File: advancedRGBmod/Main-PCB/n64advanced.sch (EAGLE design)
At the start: 110 parts, among them J5 2510-, J6 UPS, U1 10CL010YE144, U2 ADV7125/ADV7123, U4 74LVC3G17, U5 S25FLXXXSO8-DUAL, U6 TLV70012DDC, U7 TLV70025DDC

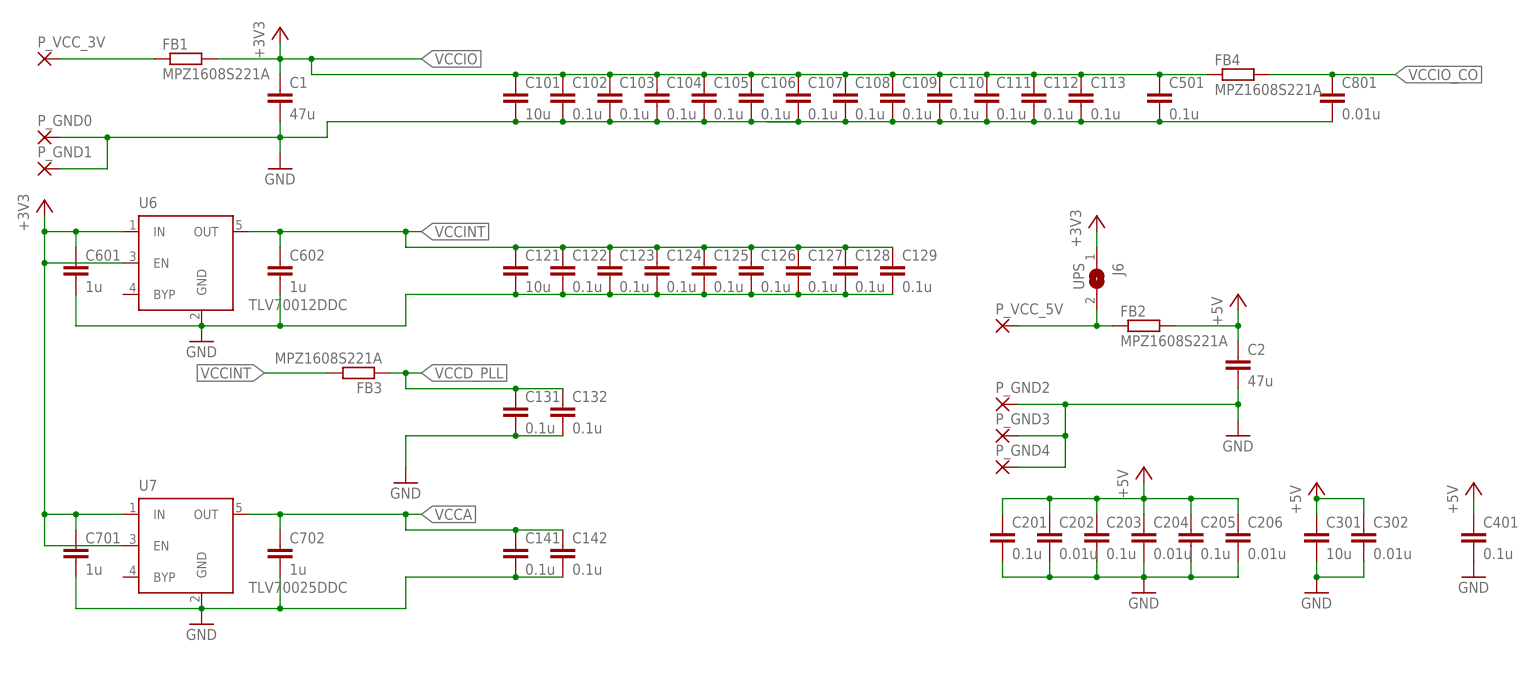
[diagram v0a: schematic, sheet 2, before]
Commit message: PCB Update: remove jumper for analog power supply I recommend 5V for the analog part anyway. So now the user is forced to use 5V here!
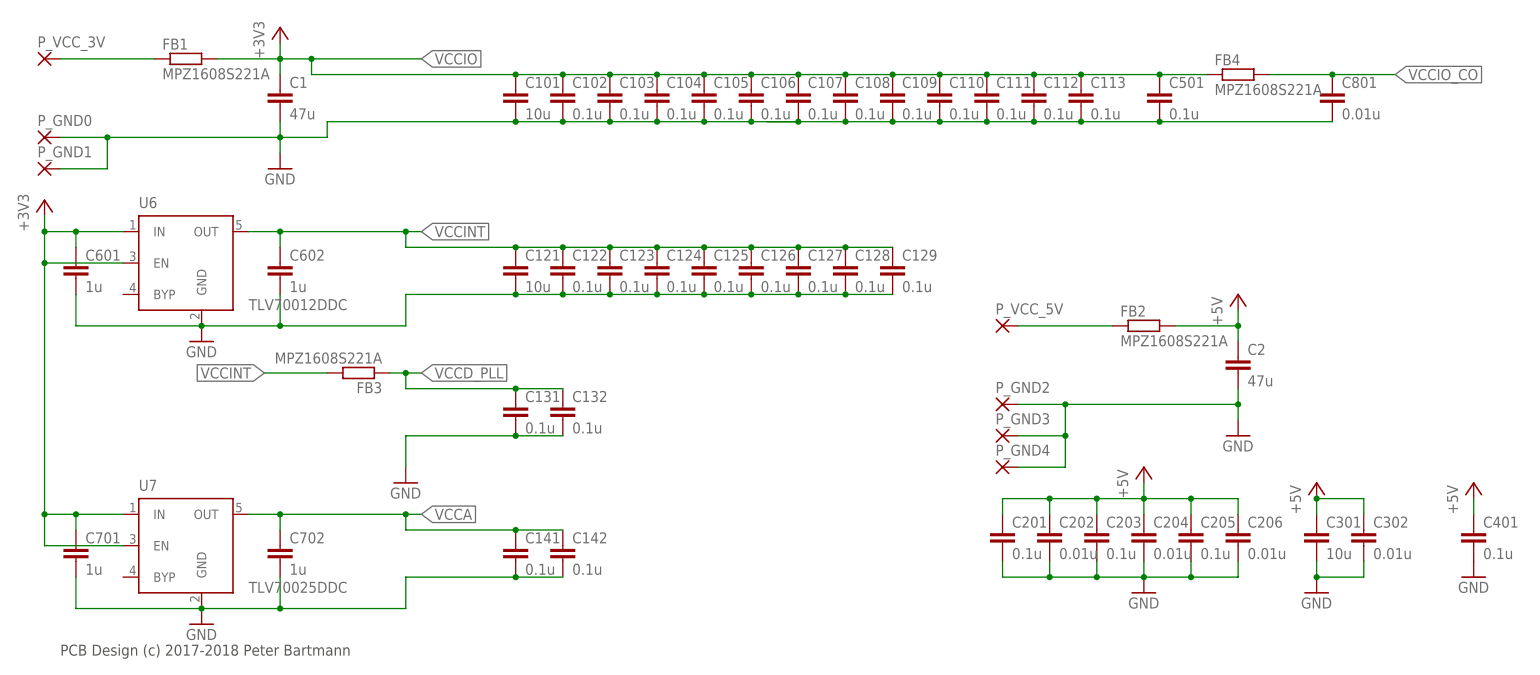
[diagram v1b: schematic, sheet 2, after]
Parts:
- removed J6: UPS, jumper:SJ
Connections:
- net N$48: no longer J6.2
- net VCCIO: no longer J6.1
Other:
- note added: "PCB Design (c) 2017-2018 Peter Bartmann"
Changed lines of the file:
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@@
 <?xml version="1.0" encoding="utf-8"?>
 <!DOCTYPE eagle SYSTEM "eagle.dtd">
-<eagle version="8.4.3">
+<eagle version="8.6.0">
 <drawing>
 <settings>
@@
 <part name="RN41" library="resistor-net" deviceset="CTS742C083" device="" value="CAY16-75R0F4LF"/>
 <part name="J4" library="jumper" deviceset="SJ2W" device=""/>
-<part name="J6" library="jumper" deviceset="SJ" device="" value="UPS"/>
 <part name="R14" library="rcl" deviceset="R-EU_" device="R0603" value="10k"/>
 <part name="AGND17" library="supply1" deviceset="GND" device=""/>
@@
 <part name="GND20" library="supply1@1" deviceset="GND" device=""/>
 <part name="+3V9" library="supply1" deviceset="+3V3" device=""/>
-<part name="+3V7" library="supply1" deviceset="+3V3" device=""/>
 <part name="C121" library="rcl" deviceset="C-EU" device="C0805" value="10u"/>
 <part name="C126" library="rcl" deviceset="C-EU" device="C0603" value="0.1u"/>
@@
 <wire x1="146.304" y1="76.962" x2="145.542" y2="77.724" width="0.1524" layer="97"/>
 <wire x1="145.542" y1="77.724" x2="145.542" y2="61.722" width="0.1524" layer="97"/>
+<text x="2.54" y="2.54" size="1.778" layer="97" font="vector">PCB Design (c) 2017-2018 Peter Bartmann</text>
 </plain>
 <instances>
@@
 <sheet>
 <plain>
+<text x="2.54" y="2.54" size="1.778" layer="97" font="vector">PCB Design (c) 2017-2018 Peter Bartmann</text>
 </plain>
 <instances>
@@
 <instance part="P_GND3" gate="1" x="154.94" y="38.1"/>
 <instance part="P_GND1" gate="1" x="0" y="81.28"/>
-<instance part="J6" gate="1" x="170.18" y="63.5" rot="R270"/>
 <instance part="GND5" gate="1" x="193.04" y="38.1"/>
 <instance part="C102" gate="G$1" x="83.82" y="93.98"/>
@@
 <instance part="C701" gate="G$1" x="5.08" y="20.32"/>
 <instance part="C702" gate="G$1" x="38.1" y="20.32"/>
-<instance part="+3V7" gate="G$1" x="170.18" y="73.66"/>
 <instance part="C121" gate="G$1" x="76.2" y="66.04"/>
 <instance part="C126" gate="G$1" x="114.3" y="66.04"/>
@@
 <pinref part="P_VCC_5V" gate="1" pin="P"/>
 <pinref part="FB2" gate="G$1" pin="1"/>
-<wire x1="157.48" y1="55.88" x2="170.18" y2="55.88" width="0.1524" layer="91"/>
-<pinref part="J6" gate="1" pin="2"/>
-<wire x1="170.18" y1="55.88" x2="172.72" y2="55.88" width="0.1524" layer="91"/>
-<wire x1="170.18" y1="58.42" x2="170.18" y2="55.88" width="0.1524" layer="91"/>
-<junction x="170.18" y="55.88"/>
+<wire x1="157.48" y1="55.88" x2="172.72" y2="55.88" width="0.1524" layer="91"/>
 </segment>
 </net>
@@
 <net name="VCCIO" class="0">
 <segment>
-<pinref part="J6" gate="1" pin="1"/>
-<pinref part="+3V7" gate="G$1" pin="+3V3"/>
-<wire x1="170.18" y1="71.12" x2="170.18" y2="68.58" width="0.1524" layer="91"/>
-</segment>
-<segment>
 <pinref part="C111" gate="G$1" pin="1"/>

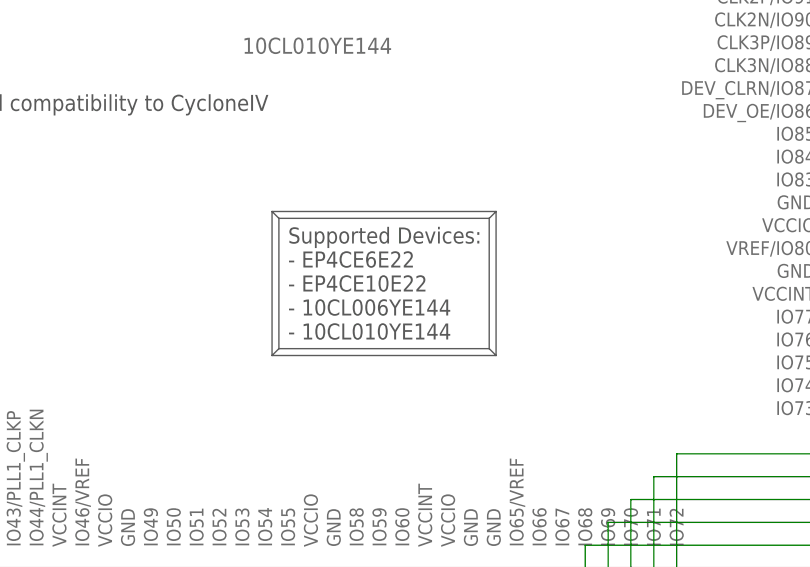
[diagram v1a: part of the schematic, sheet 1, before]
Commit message: discontinue 6k LE FPGA support for now
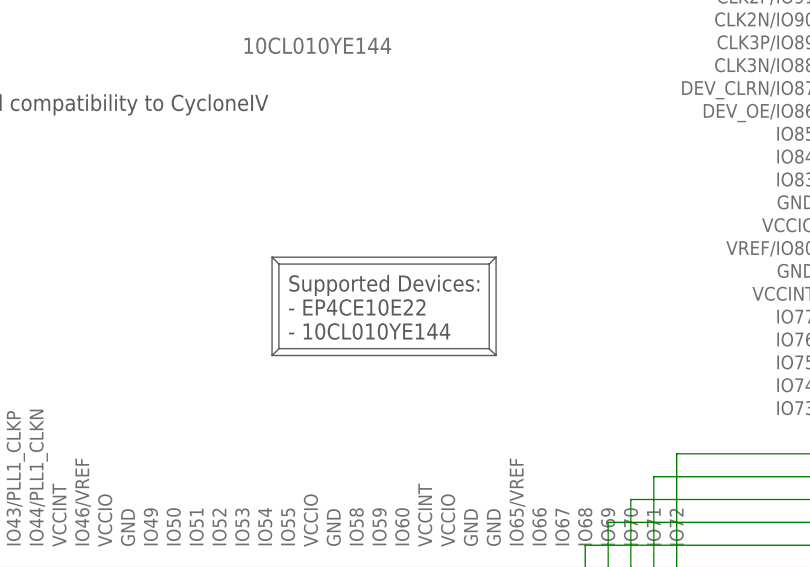
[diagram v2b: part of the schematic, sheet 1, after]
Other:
- note added: "Supported Devices: - EP4CE10E22 - 10CL010YE144"
- note removed: "Supported Devices: - EP4CE6E22 - EP4CE10E22 - 10CL006YE144 - 10CL010YE144"
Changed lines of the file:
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@@
 <?xml version="1.0" encoding="utf-8"?>
 <!DOCTYPE eagle SYSTEM "eagle.dtd">
-<eagle version="8.6.0">
+<eagle version="8.7.1">
 <drawing>
 <settings>
@@
 -&gt; Backward compatibility to CycloneIV</text>
 <text x="147.32" y="63.5" size="1.778" layer="97">Supported Devices:
-- EP4CE6E22
 - EP4CE10E22
-- 10CL006YE144
 - 10CL010YE144</text>
 <wire x1="146.304" y1="62.484" x2="169.672" y2="62.484" width="0.1524" layer="97"/>
-<wire x1="169.672" y1="62.484" x2="169.672" y2="76.962" width="0.1524" layer="97"/>
-<wire x1="169.672" y1="76.962" x2="146.304" y2="76.962" width="0.1524" layer="97"/>
-<wire x1="146.304" y1="76.962" x2="146.304" y2="62.484" width="0.1524" layer="97"/>
+<wire x1="169.672" y1="62.484" x2="169.672" y2="71.882" width="0.1524" layer="97"/>
+<wire x1="169.672" y1="71.882" x2="146.304" y2="71.882" width="0.1524" layer="97"/>
+<wire x1="146.304" y1="71.882" x2="146.304" y2="62.484" width="0.1524" layer="97"/>
 <wire x1="146.304" y1="62.484" x2="145.542" y2="61.722" width="0.1524" layer="97"/>
 <wire x1="145.542" y1="61.722" x2="170.434" y2="61.722" width="0.1524" layer="97"/>
 <wire x1="169.672" y1="62.484" x2="170.434" y2="61.722" width="0.1524" layer="97"/>
-<wire x1="170.434" y1="61.722" x2="170.434" y2="77.724" width="0.1524" layer="97"/>
-<wire x1="169.672" y1="76.962" x2="170.434" y2="77.724" width="0.1524" layer="97"/>
-<wire x1="170.434" y1="77.724" x2="145.542" y2="77.724" width="0.1524" layer="97"/>
-<wire x1="146.304" y1="76.962" x2="145.542" y2="77.724" width="0.1524" layer="97"/>
-<wire x1="145.542" y1="77.724" x2="145.542" y2="61.722" width="0.1524" layer="97"/>
+<wire x1="170.434" y1="61.722" x2="170.434" y2="72.644" width="0.1524" layer="97"/>
+<wire x1="169.672" y1="71.882" x2="170.434" y2="72.644" width="0.1524" layer="97"/>
+<wire x1="170.434" y1="72.644" x2="145.542" y2="72.644" width="0.1524" layer="97"/>
+<wire x1="146.304" y1="71.882" x2="145.542" y2="72.644" width="0.1524" layer="97"/>
+<wire x1="145.542" y1="72.644" x2="145.542" y2="61.722" width="0.1524" layer="97"/>
 <text x="2.54" y="2.54" size="1.778" layer="97" font="vector">PCB Design (c) 2017-2018 Peter Bartmann</text>
 </plain>

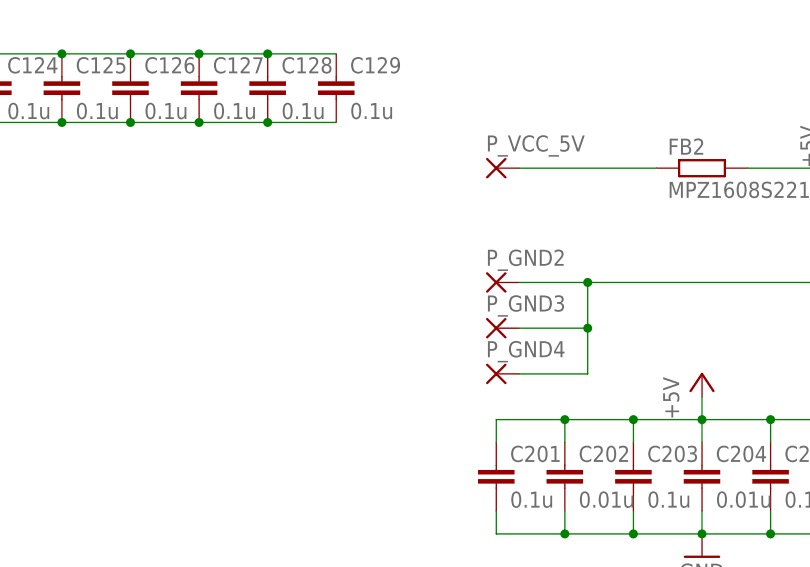
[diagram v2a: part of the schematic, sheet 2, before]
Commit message: update PCB - add fields for GND shield fingers and remove pad for /COLD
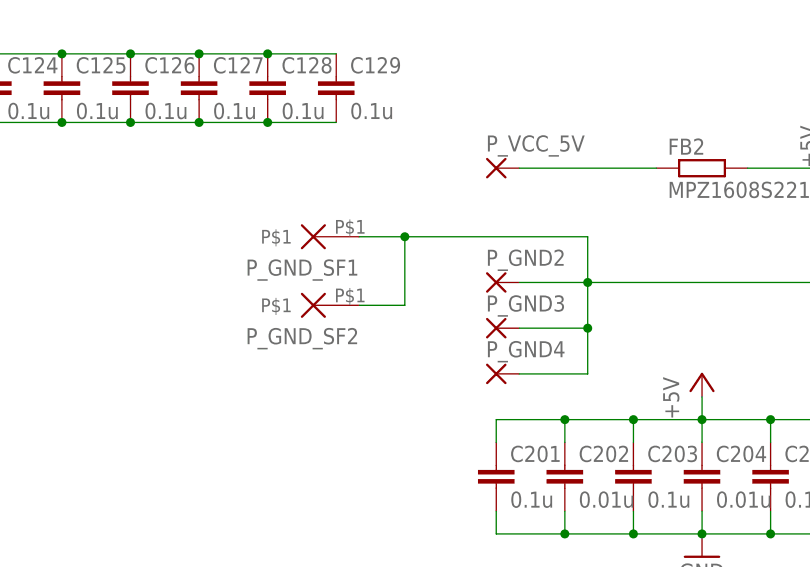
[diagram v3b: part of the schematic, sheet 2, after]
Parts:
- removed /COLD: (no value), wirepad@1:SMD2
- added P_GND_SF1, P_GND_SF2: PADSHIELD_FINGER, snes_div:PADSHIELD_FINGER
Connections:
- removed net N$56: RN12.7, U1.IO128
- removed net N$67: /COLD.P, RN12.2
- net GND: now also P_GND_SF1.P$1, P_GND_SF2.P$1
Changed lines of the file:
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@@
 <?xml version="1.0" encoding="utf-8"?>
 <!DOCTYPE eagle SYSTEM "eagle.dtd">
-<eagle version="8.7.1">
+<eagle version="9.0.1">
 <drawing>
 <settings>
@@
 <part name="CTRL" library="wirepad@1" deviceset="SMD2" device=""/>
 <part name="/RST" library="wirepad@1" deviceset="SMD2" device=""/>
-<part name="/COLD" library="wirepad@1" deviceset="SMD2" device=""/>
 <part name="GND1" library="supply1" deviceset="GND" device=""/>
 <part name="C801" library="rcl" deviceset="C-EU" device="C0603" value="0.01u"/>
@@
 <part name="+3V12" library="supply1" deviceset="+3V3" device=""/>
 <part name="P_GND4" library="wirepad@1" deviceset="SMD2" device=""/>
+<part name="P_GND_SF1" library="snes_div" deviceset="PAD" device="SHIELD_FINGER" value=""/>
+<part name="P_GND_SF2" library="snes_div" deviceset="PAD" device="SHIELD_FINGER" value=""/>
 </parts>
 <sheets>
@@
 <instance part="CTRL" gate="1" x="144.78" y="208.28" rot="R270"/>
 <instance part="/RST" gate="1" x="139.7" y="223.52" rot="R270"/>
-<instance part="/COLD" gate="1" x="142.24" y="215.9" rot="R270"/>
 <instance part="GND1" gate="1" x="17.78" y="71.12"/>
 <instance part="RN23" gate="G$1" x="398.78" y="17.78" rot="R270"/>
@@
 </segment>
 </net>
-<net name="N$56" class="0">
-<segment>
-<pinref part="RN12" gate="G$1" pin="7"/>
-<wire x1="142.24" y1="190.5" x2="142.24" y2="167.64" width="0.1524" layer="91"/>
-<pinref part="U1" gate="G$1" pin="IO128"/>
-</segment>
-</net>
 <net name="N$57" class="0">
 <segment>
@@
 <pinref part="CTRL" gate="1" pin="P"/>
 <wire x1="144.78" y1="203.2" x2="144.78" y2="205.74" width="0.1524" layer="91"/>
-</segment>
-</net>
-<net name="N$67" class="0">
-<segment>
-<pinref part="/COLD" gate="1" pin="P"/>
-<pinref part="RN12" gate="G$1" pin="2"/>
-<wire x1="142.24" y1="213.36" x2="142.24" y2="203.2" width="0.1524" layer="91"/>
 </segment>
 </net>
@@
 <instance part="FB4" gate="G$1" x="193.04" y="96.52"/>
 <instance part="P_GND4" gate="1" x="154.94" y="33.02"/>
+<instance part="P_GND_SF1" gate="G$1" x="137.16" y="48.26" rot="R180"/>
+<instance part="P_GND_SF2" gate="G$1" x="137.16" y="40.64" rot="R180"/>
 </instances>
 <busses>
@@
 <wire x1="165.1" y1="33.02" x2="165.1" y2="38.1" width="0.1524" layer="91"/>
 <junction x="165.1" y="38.1"/>
-</segment>
-<segment>
+<pinref part="P_GND_SF1" gate="G$1" pin="P$1"/>
+<wire x1="139.7" y1="48.26" x2="144.78" y2="48.26" width="0.1524" layer="91"/>
+<wire x1="144.78" y1="48.26" x2="165.1" y2="48.26" width="0.1524" layer="91"/>
+<wire x1="165.1" y1="48.26" x2="165.1" y2="43.18" width="0.1524" layer="91"/>
+<pinref part="P_GND_SF2" gate="G$1" pin="P$1"/>
+<wire x1="139.7" y1="40.64" x2="144.78" y2="40.64" width="0.1524" layer="91"/>
+<wire x1="144.78" y1="40.64" x2="144.78" y2="48.26" width="0.1524" layer="91"/>
+<junction x="144.78" y="48.26"/>
+</segment>
+<segment>
